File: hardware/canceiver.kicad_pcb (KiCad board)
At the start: 2 copper layers, 33.2 x 48.4 mm, 32 parts, among them J1 LD09P13A4GV00LF, J2 629105150521, J3 TC2030-IDC-NL, U1 NCP730ASN330, U2 USBLC6-2SC6, U3 STM32F303RCTx, U4 ADM3058E, U5 NCP730ASN500, Y1 ECS-80-18-30-JGN

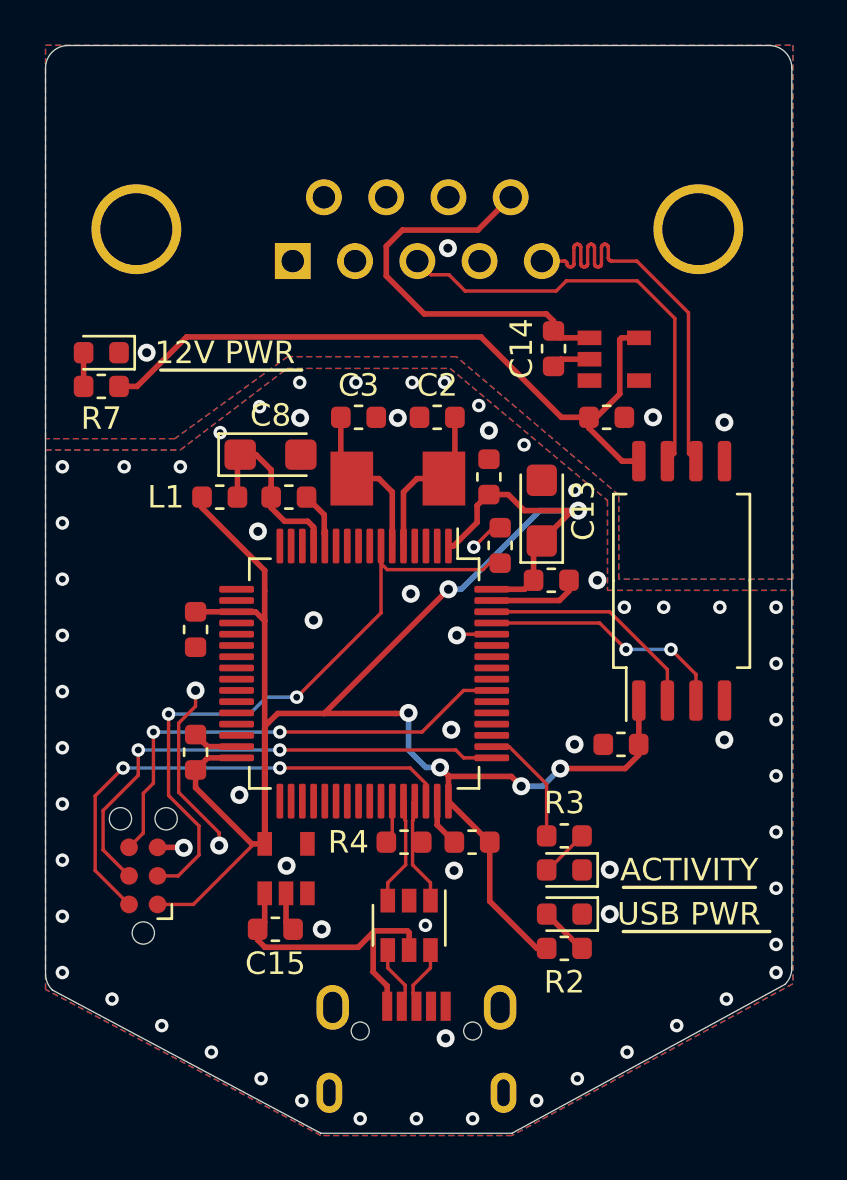
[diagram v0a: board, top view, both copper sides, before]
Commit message: upgrade to kicad 7
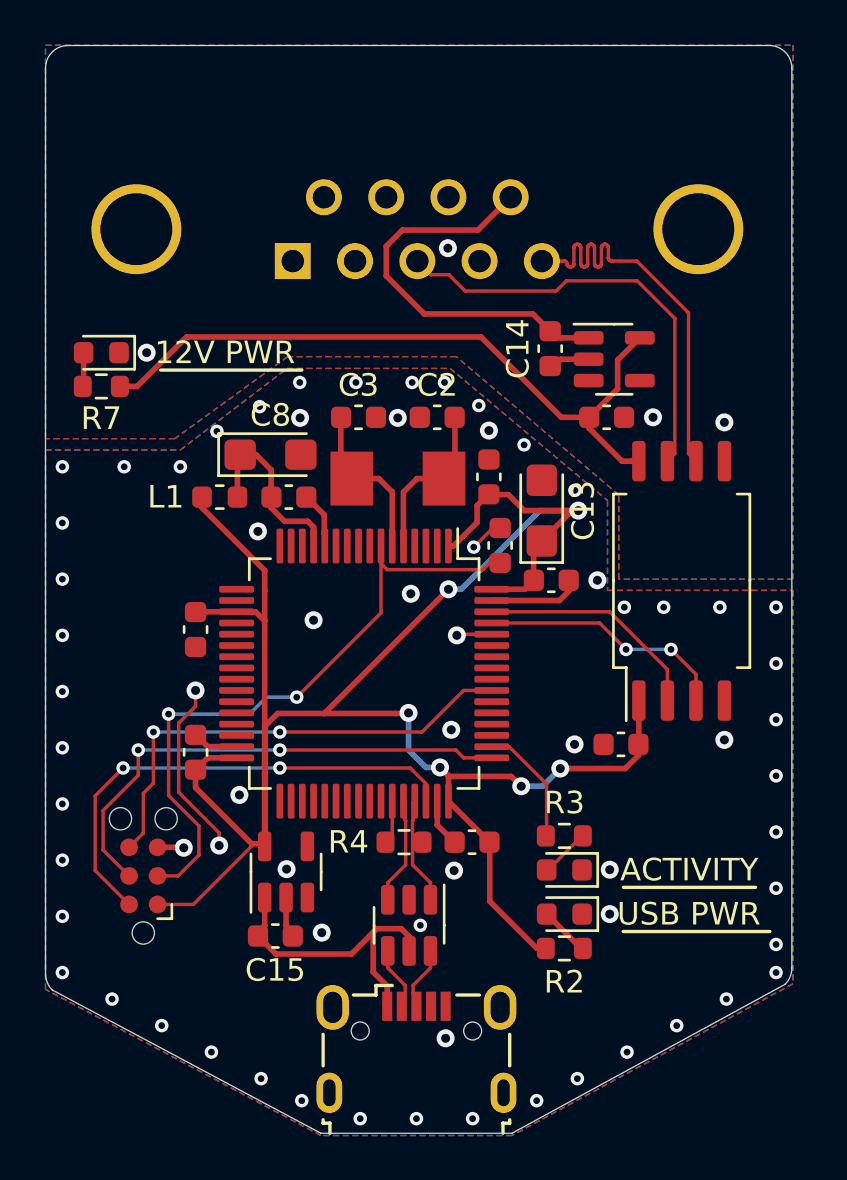
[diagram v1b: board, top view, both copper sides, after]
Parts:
- C2, C3: value 22pF -> 26pF
- moved C15 0.30 mm to (144.2, 100.6)
- moved C14 0.15 mm to (156.4, 74.5)
- moved U1 0.15 mm to (144.7, 97.8)
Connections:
- J1 pad 4: Net-(J1-Pad4) -> unconnected-(J1-Pad4)
- J1 pad 6: Net-(J1-Pad6) -> unconnected-(J1-Pad6)
- J1 pad 7: Net-(J1-Pad7) -> unconnected-(J1-Pad7)
- J1 pad 8: Net-(J1-Pad8) -> unconnected-(J1-Pad8)
- J2 pad 4: Net-(J2-Pad4) -> unconnected-(J2-ID-Pad4)
- J2 pad 6: Net-(J2-Pad6) -> unconnected-(J2-Shield-Pad6)
- U1 pad 3: Net-(U1-Pad3) -> unconnected-(U1-EN-Pad3)
- U1 pad 4: Net-(U1-Pad4) -> unconnected-(U1-NC-Pad4)
- U3 pad 10: Net-(U3-Pad10) -> unconnected-(U3-PC2-Pad10)
- U3 pad 11: Net-(U3-Pad11) -> unconnected-(U3-PC3-Pad11)
- U3 pad 14: Net-(U3-Pad14) -> unconnected-(U3-PA0-Pad14)
- U3 pad 15: Net-(U3-Pad15) -> unconnected-(U3-PA1-Pad15)
- U3 pad 16: Net-(U3-Pad16) -> unconnected-(U3-PA2-Pad16)
- U3 pad 17: Net-(U3-Pad17) -> unconnected-(U3-PA3-Pad17)
- U3 pad 18: Net-(U3-Pad18) -> unconnected-(U3-PF4-Pad18)
- U3 pad 2: Net-(U3-Pad2) -> unconnected-(U3-PC13-Pad2)
- U3 pad 20: Net-(U3-Pad20) -> unconnected-(U3-PA4-Pad20)
- U3 pad 21: Net-(U3-Pad21) -> unconnected-(U3-PA5-Pad21)
- U3 pad 22: Net-(U3-Pad22) -> unconnected-(U3-PA6-Pad22)
- U3 pad 23: Net-(U3-Pad23) -> unconnected-(U3-PA7-Pad23)
- U3 pad 24: Net-(U3-Pad24) -> unconnected-(U3-PC4-Pad24)
- U3 pad 25: Net-(U3-Pad25) -> unconnected-(U3-PC5-Pad25)
- U3 pad 26: Net-(U3-Pad26) -> unconnected-(U3-PB0-Pad26)
- U3 pad 27: Net-(U3-Pad27) -> unconnected-(U3-PB1-Pad27)
- U3 pad 28: Net-(U3-Pad28) -> unconnected-(U3-PB2-Pad28)
- U3 pad 29: Net-(U3-Pad29) -> unconnected-(U3-PB10-Pad29)
- U3 pad 3: Net-(U3-Pad3) -> unconnected-(U3-PC14-Pad3)
- U3 pad 30: Net-(U3-Pad30) -> unconnected-(U3-PB11-Pad30)
- U3 pad 33: Net-(U3-Pad33) -> unconnected-(U3-PB12-Pad33)
- U3 pad 34: Net-(U3-Pad34) -> unconnected-(U3-PB13-Pad34)
- U3 pad 35: Net-(U3-Pad35) -> unconnected-(U3-PB14-Pad35)
- U3 pad 36: Net-(U3-Pad36) -> unconnected-(U3-PB15-Pad36)
- U3 pad 37: Net-(U3-Pad37) -> unconnected-(U3-PC6-Pad37)
- U3 pad 38: Net-(U3-Pad38) -> unconnected-(U3-PC7-Pad38)
- U3 pad 39: Net-(U3-Pad39) -> unconnected-(U3-PC8-Pad39)
- U3 pad 4: Net-(U3-Pad4) -> unconnected-(U3-PC15-Pad4)
- U3 pad 40: Net-(U3-Pad40) -> unconnected-(U3-PC9-Pad40)
- U3 pad 41: Net-(U3-Pad41) -> unconnected-(U3-PA8-Pad41)
- U3 pad 42: Net-(U3-Pad42) -> unconnected-(U3-PA9-Pad42)
- U3 pad 51: Net-(U3-Pad51) -> unconnected-(U3-PC10-Pad51)
- U3 pad 52: Net-(U3-Pad52) -> unconnected-(U3-PC11-Pad52)
- U3 pad 53: Net-(U3-Pad53) -> unconnected-(U3-PC12-Pad53)
- U3 pad 54: Net-(U3-Pad54) -> unconnected-(U3-PD2-Pad54)
- U3 pad 56: Net-(U3-Pad56) -> unconnected-(U3-PB4-Pad56)
- U3 pad 57: Net-(U3-Pad57) -> unconnected-(U3-PB5-Pad57)
- U3 pad 58: Net-(U3-Pad58) -> unconnected-(U3-PB6-Pad58)
- U3 pad 59: Net-(U3-Pad59) -> unconnected-(U3-PB7-Pad59)
- U3 pad 8: Net-(U3-Pad8) -> unconnected-(U3-PC0-Pad8)
- U3 pad 9: Net-(U3-Pad9) -> unconnected-(U3-PC1-Pad9)
- U5 pad 3: Net-(U5-Pad3) -> unconnected-(U5-EN-Pad3)
- U5 pad 4: Net-(U5-Pad4) -> unconnected-(U5-NC-Pad4)
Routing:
- net +5V: track 31.7 -> 31.1 mm
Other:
- net class CAN removed
- net class Default removed
- net class USB removed
